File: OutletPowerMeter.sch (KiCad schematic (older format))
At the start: 94 parts, among them J1 TB002-500-03BE, J2 TB002V-500-03BE, J3 OLED, J4 Programmer, J5 TB002V-500-02BE, SW1 PTS647SN70SMTR2LFS, T1 115V / 9V, U1 ESP32-DEVKITC-32D, U10 ADG3304BRUZ-REEL7, U11 VX7803-500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

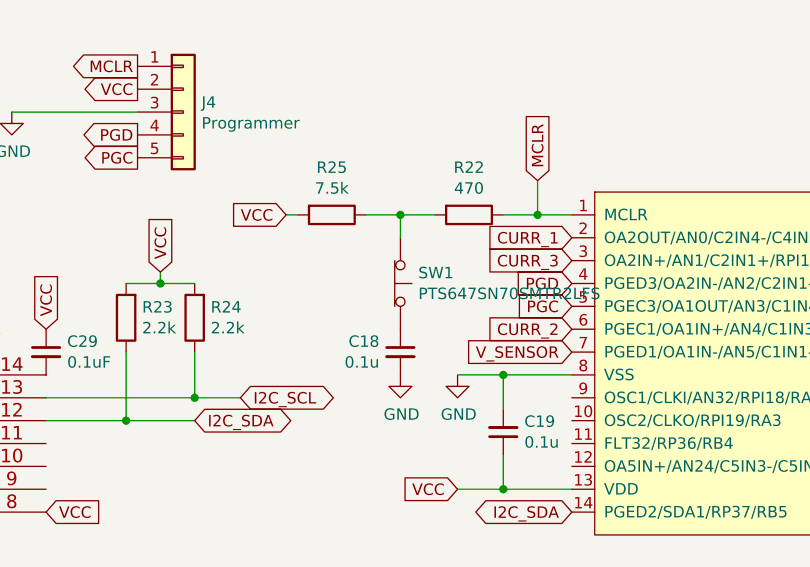
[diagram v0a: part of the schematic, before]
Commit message: Updated tactile switch and various footprints like current sensors and caps
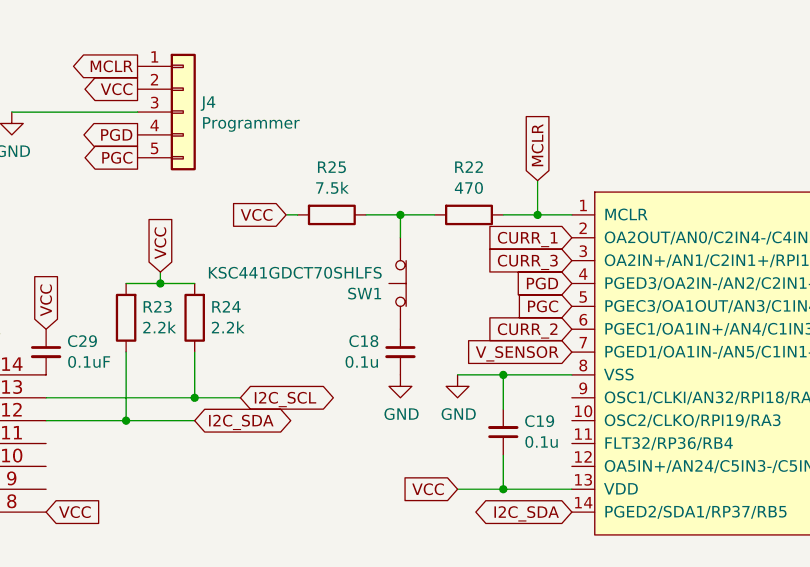
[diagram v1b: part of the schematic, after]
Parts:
- C1: footprint Capacitor_THT:C_Rect_L7.2mm_W3.5mm_P5.00mm_FKS2_FKP2_MKS2_MKP2 -> MyCustom_Footprints:C_Rect_L19.0mm_W10.0mm_P15.00mm_MKS4
- C2: footprint Capacitor_THT:C_Rect_L13.0mm_W5.0mm_P10.00mm_FKS3_FKP3_MKS4 -> Capacitor_THT:C_Rect_L7.2mm_W3.5mm_P5.00mm_FKS2_FKP2_MKS2_MKP2
- R1, R2, R3, R4, R5, R6: footprint Varistor:RV_Disc_D12mm_W3.9mm_P7.5mm -> MyCustom_Footprints:RV_Disc_D12mm_W3.9mm_P7.5mm_1.1mm
- SW1: value PTS647SN70SMTR2LFS -> KSC441GDCT70SHLFS; footprint (none) -> MyCustom_Footprints:KSC4
- U5, U6, U7: footprint SOIC-8_ALM -> Package_SO:SOIC-8_3.9x4.9mm_P1.27mm
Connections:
- net at R22.2, R25.1: now also SW1.2 (B); no longer SW1.1 (A)
- net at C18.1: now also SW1.1 (A); no longer SW1.2 (B)
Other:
- moved on the sheet: SW1
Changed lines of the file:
@@
 F 0 "R4" H 2300 2050 50  0000 R CNN
 F 1 "MOV-10D201KTR" H 2100 2600 50  0001 R CNN
-F 2 "Varistor:RV_Disc_D12mm_W3.9mm_P7.5mm" V 2080 2100 50  0001 C CNN
+F 2 "MyCustom_Footprints:RV_Disc_D12mm_W3.9mm_P7.5mm_1.1mm" V 2080 2100 50  0001 C CNN
 F 3 "~" H 2150 2100 50  0001 C CNN
 	1    2150 2100
@@
 F 0 "R1" H 1550 1750 50  0000 R CNN
 F 1 "MOV-10D201KTR" H 1350 2300 50  0001 R CNN
-F 2 "Varistor:RV_Disc_D12mm_W3.9mm_P7.5mm" V 1330 1800 50  0001 C CNN
+F 2 "MyCustom_Footprints:RV_Disc_D12mm_W3.9mm_P7.5mm_1.1mm" V 1330 1800 50  0001 C CNN
 F 3 "~" H 1400 1800 50  0001 C CNN
 	1    1400 1800
@@
 F 0 "R5" H 2550 1900 50  0000 R CNN
 F 1 "MOV-10D201KTR" H 2950 2350 50  0000 R CNN
-F 2 "Varistor:RV_Disc_D12mm_W3.9mm_P7.5mm" V 2330 1950 50  0001 C CNN
+F 2 "MyCustom_Footprints:RV_Disc_D12mm_W3.9mm_P7.5mm_1.1mm" V 2330 1950 50  0001 C CNN
 F 3 "~" H 2400 1950 50  0001 C CNN
 	1    2400 1950
@@
 F 0 "R2" H 1800 1750 50  0000 R CNN
 F 1 "MOV-10D201KTR" H 1600 2300 50  0001 R CNN
-F 2 "Varistor:RV_Disc_D12mm_W3.9mm_P7.5mm" V 1580 1800 50  0001 C CNN
+F 2 "MyCustom_Footprints:RV_Disc_D12mm_W3.9mm_P7.5mm_1.1mm" V 1580 1800 50  0001 C CNN
 F 3 "~" H 1650 1800 50  0001 C CNN
 	1    1650 1800
@@
 F 0 "R3" H 2050 2050 50  0000 R CNN
 F 1 "MOV-10D201KTR" H 1850 2600 50  0001 R CNN
-F 2 "Varistor:RV_Disc_D12mm_W3.9mm_P7.5mm" V 1830 2100 50  0001 C CNN
+F 2 "MyCustom_Footprints:RV_Disc_D12mm_W3.9mm_P7.5mm_1.1mm" V 1830 2100 50  0001 C CNN
 F 3 "~" H 1900 2100 50  0001 C CNN
 	1    1900 2100
@@
 F 0 "R6" H 2800 1900 50  0000 R CNN
 F 1 "MOV-10D201KTR" H 3200 2350 50  0001 R CNN
-F 2 "Varistor:RV_Disc_D12mm_W3.9mm_P7.5mm" V 2580 1950 50  0001 C CNN
+F 2 "MyCustom_Footprints:RV_Disc_D12mm_W3.9mm_P7.5mm_1.1mm" V 2580 1950 50  0001 C CNN
 F 3 "~" H 2650 1950 50  0001 C CNN
 	1    2650 1950
@@
 F 0 "U5" H 8700 1938 60  0000 C CNN
 F 1 "ACS712ELCTR-20A-T" H 8700 1832 60  0000 C CNN
-F 2 "SOIC-8_ALM" H 8700 1790 60  0001 C CNN
+F 2 "Package_SO:SOIC-8_3.9x4.9mm_P1.27mm" H 8700 1790 60  0001 C CNN
 F 3 "" H 7500 1550 60  0000 C CNN
 	1    7500 1550
@@
 F 0 "U6" H 8700 3438 60  0000 C CNN
 F 1 "ACS712ELCTR-20A-T" H 8700 3332 60  0000 C CNN
-F 2 "SOIC-8_ALM" H 8700 3290 60  0001 C CNN
+F 2 "Package_SO:SOIC-8_3.9x4.9mm_P1.27mm" H 8700 3290 60  0001 C CNN
 F 3 "" H 7500 3050 60  0000 C CNN
 	1    7500 3050
@@
 F 0 "U7" H 8700 5038 60  0000 C CNN
 F 1 "ACS712ELCTR-20A-T" H 8700 4932 60  0000 C CNN
-F 2 "SOIC-8_ALM" H 8700 4890 60  0001 C CNN
+F 2 "Package_SO:SOIC-8_3.9x4.9mm_P1.27mm" H 8700 4890 60  0001 C CNN
 F 3 "" H 7500 4650 60  0000 C CNN
 	1    7500 4650
@@
 F 0 "C2" H 2192 5946 50  0000 L CNN
 F 1 "6.8nF/275V" H 2192 5855 50  0000 L CNN
-F 2 "Capacitor_THT:C_Rect_L13.0mm_W5.0mm_P10.00mm_FKS3_FKP3_MKS4" H 2100 5900 50  0001 C CNN
+F 2 "Capacitor_THT:C_Rect_L7.2mm_W3.5mm_P5.00mm_FKS2_FKP2_MKS2_MKP2" H 2100 5900 50  0001 C CNN
 F 3 "~" H 2100 5900 50  0001 C CNN
 	1    2100 5900
@@
 F 0 "C1" H 1442 5946 50  0000 L CNN
 F 1 "100nF/250V" H 1442 5855 50  0000 L CNN
-F 2 "Capacitor_THT:C_Rect_L7.2mm_W3.5mm_P5.00mm_FKS2_FKP2_MKS2_MKP2" H 1350 5900 50  0001 C CNN
+F 2 "MyCustom_Footprints:C_Rect_L19.0mm_W10.0mm_P15.00mm_MKS4" H 1350 5900 50  0001 C CNN
 F 3 "~" H 1350 5900 50  0001 C CNN
 	1    1350 5900
@@
 P 6350 9200
 F 0 "SW1" V 6304 9278 50  0000 L CNN
-F 1 "PTS647SN70SMTR2LFS" V 6395 9278 50  0000 L CNN
-F 2 "" H 6350 9400 50  0001 C CNN
+F 1 "KSC441GDCT70SHLFS" V 6395 9278 50  0000 L CNN
+F 2 "MyCustom_Footprints:KSC4" H 6350 9400 50  0001 C CNN
 F 3 "~" H 6350 9400 50  0001 C CNN
 	1    6350 9200
-	0    1    1    0
+	0    -1   -1   0
 $EndComp
 Connection ~ 5450 9700

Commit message: Fixed Vcc capacitors. Added more vias.
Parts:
- removed C32: 0.1uF, Capacitor_SMD:C_0805_2012Metric_Pad1.15x1.40mm_HandSolder, symbol Device:C_Small
- added C25: 0.1uF, Capacitor_SMD:C_0805_2012Metric_Pad1.15x1.40mm_HandSolder, symbol Device:C_Small
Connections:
- net 3V3: now also U10.1 (VCCA)
- net GND: now also C24.2, C26.2, C27.1, C28.2, C29.2, C30.2, C31.2, C25.2
- net VCC: now also C24.1, C28.1, C30.1, C31.1, U1.19 (EXT_5V), U10.14 (VCCY), U5.8 (VCC), U6.8 (VCC), U7.8 (VCC), U8.8 (VDD), U9.5, C25.1; no longer C24.2, C28.2, C30.2, C31.2
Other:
- moved on the sheet: C24, C26, C27, C28, C29, C30

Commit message: Changed capacitor footprint to 1210 as well as the symbol.
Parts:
- C6: footprint Capacitor_SMD:C_1206_3216Metric_Pad1.42x1.75mm_HandSolder -> Capacitor_Tantalum_SMD:CP_EIA-3528-21_Kemet-B_Pad1.50x2.35mm_HandSolder; symbol Device:C_Small -> Device:CP1_Small
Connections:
- net at R7.2, R8.1: now also C6.1; no longer C6.2
- net at D2.3, R10.2, R11.1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: now also C6.2; no longer C6.1
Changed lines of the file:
@@
 	700  7100 700  7200
 $Comp
-L Device:C_Small C6
+L Device:CP1_Small C6
 U 1 1 5EEE7C78
 P 1050 7200
 F 0 "C6" H 1142 7246 50  0000 L CNN
 F 1 "100u" H 1142 7155 50  0000 L CNN
-F 2 "Capacitor_SMD:C_1206_3216Metric_Pad1.42x1.75mm_HandSolder" H 1050 7200 50  0001 C CNN
+F 2 "Capacitor_Tantalum_SMD:CP_EIA-3528-21_Kemet-B_Pad1.50x2.35mm_HandSolder" H 1050 7200 50  0001 C CNN
 F 3 "~" H 1050 7200 50  0001 C CNN
 	1    1050 7200
-	0    1    1    0
+	0    -1   -1   0
 $EndComp
 $Comp

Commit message: Revision 1 completed. Order sent to JLCPCB. Routed traces, rearranged components, and changed footprints.
	new file:   Gerber.zip
	modified:   OutletPowerMeter.kicad_pcb
	modified:   OutletPowerMeter.kicad_pcb-bak
	modified:   OutletPowerMeter.net
	modified:   OutletPowerMeter.sch
	modified:   OutletPowerMeter.sch-bak
	modified:   OutletPowerMeter.xml
	modified:   OutletPowerMeter.zip
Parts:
- C10, C14, C15, C16: footprint Capacitor_SMD:C_1206_3216Metric_Pad1.42x1.75mm_HandSolder -> Capacitor_SMD:C_0805_2012Metric_Pad1.15x1.40mm_HandSolder
- U10: footprint RU_14_ADI -> Package_SO:TSSOP-14_4.4x5mm_P0.65mm
- U8: footprint SOIC8-N_MC_MCH -> Package_SO:SOIC-8_3.9x4.9mm_P1.27mm
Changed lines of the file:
@@
 F 0 "C14" H 12892 1796 50  0000 L CNN
 F 1 "100n" H 12892 1705 50  0000 L CNN
-F 2 "Capacitor_SMD:C_1206_3216Metric_Pad1.42x1.75mm_HandSolder" H 12800 1750 50  0001 C CNN
+F 2 "Capacitor_SMD:C_0805_2012Metric_Pad1.15x1.40mm_HandSolder" H 12800 1750 50  0001 C CNN
 F 3 "~" H 12800 1750 50  0001 C CNN
 	1    12800 1750
@@
 F 0 "U10" H 4100 9850 60  0000 C CNN
 F 1 "ADG3304BRUZ-REEL7" H 4150 9750 60  0000 C CNN
-F 2 "RU_14_ADI" H 4650 9740 60  0001 C CNN
+F 2 "Package_SO:TSSOP-14_4.4x5mm_P0.65mm" H 4650 9740 60  0001 C CNN
 F 3 "" H 3450 9600 60  0000 C CNN
 	1    3450 9600
@@
 F 0 "U8" H 3350 3287 60  0000 C CNN
 F 1 "MCP6542T-I_SN" H 3350 3181 60  0000 C CNN
-F 2 "SOIC8-N_MC_MCH" H 3350 3140 60  0001 C CNN
+F 2 "Package_SO:SOIC-8_3.9x4.9mm_P1.27mm" H 3350 3140 60  0001 C CNN
 F 3 "" H 2550 3000 60  0000 C CNN
 	1    2550 3000
@@
 F 0 "C15" H 12892 3296 50  0000 L CNN
 F 1 "100n" H 12892 3205 50  0000 L CNN
-F 2 "Capacitor_SMD:C_1206_3216Metric_Pad1.42x1.75mm_HandSolder" H 12800 3250 50  0001 C CNN
+F 2 "Capacitor_SMD:C_0805_2012Metric_Pad1.15x1.40mm_HandSolder" H 12800 3250 50  0001 C CNN
 F 3 "~" H 12800 3250 50  0001 C CNN
 	1    12800 3250
@@
 F 0 "C16" H 12892 4896 50  0000 L CNN
 F 1 "100n" H 12892 4805 50  0000 L CNN
-F 2 "Capacitor_SMD:C_1206_3216Metric_Pad1.42x1.75mm_HandSolder" H 12800 4850 50  0001 C CNN
+F 2 "Capacitor_SMD:C_0805_2012Metric_Pad1.15x1.40mm_HandSolder" H 12800 4850 50  0001 C CNN
 F 3 "~" H 12800 4850 50  0001 C CNN
 	1    12800 4850
@@
 F 0 "C10" H 3692 7346 50  0000 L CNN
 F 1 "100n" H 3692 7255 50  0000 L CNN
-F 2 "Capacitor_SMD:C_1206_3216Metric_Pad1.42x1.75mm_HandSolder" H 3600 7300 50  0001 C CNN
+F 2 "Capacitor_SMD:C_0805_2012Metric_Pad1.15x1.40mm_HandSolder" H 3600 7300 50  0001 C CNN
 F 3 "~" H 3600 7300 50  0001 C CNN
 	1    3600 7300

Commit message: Updated schematic to make it more 'linear' and added the 27k resistors for power factor circuitry
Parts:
- added R? (x2): 27k, Resistor_SMD:R_1206_3216Metric_Pad1.42x1.75mm_HandSolder, symbol Device:R
- D1: symbol Diode_Bridge:MB2S -> Device:D_Bridge_+-AA
- J4: value Programmer -> dsPIC33 Programmer
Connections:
- net GND: now also D1.2 (-), R?.2, R?.2; no longer D1.4 (-)
- net at C22.1, C3.1, C4.1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: now also D1.1 (+); no longer D1.3 (+)
- net at C6.2, D2.3, R10.2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: now also U3.3 (+); no longer U3.2 (-)
- net at R12.2, U3.1: now also U3.2 (-); no longer U3.3 (+)
- net at D5.3, R15.1: now also U3.12 (+); no longer U3.13 (-)
- net at D4.3, R14.1: now also U3.10 (+); no longer U3.9 (-)
- net at D3.3, R13.1: now also U3.5 (+); no longer U3.6 (-)
- net at R16.2, U3.7: now also U3.6 (-); no longer U3.5 (+)
- net at R17.2, U3.8: now also U3.9 (-); no longer U3.10 (+)
- net at R18.2, U3.14: now also U3.13 (-); no longer U3.12 (+)
- net at C2.1, T1.9 (SA): now also D1.4 (~~); no longer D1.1 (~~)
- net at D6.1 (K), D8.2 (A), U8.2 (VINA-): now also R20.2, R?.1; no longer R20.1
- net at D6.2 (A), D8.1 (K), R21.2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: now also R?.1
- net 9V: no longer names the net of R7.1, T1.7 (SB), TP1.1
- net 9V: now also D1.3 (~~); no longer D1.2 (~~)
- net HOT_LEAD renamed HOT_WIRE_INPUT
- net HOT_OUT: no longer names the net of C1.1, C8.1, FL1.4, J2.2 (Pin_2), R21.1, T1.5 (AA)
- net I2C_SCL_3V3 renamed SCL_3.3V
- net SCL_3.3V: now also J3.1 (Pin_1); no longer J3.2 (Pin_2)
- net I2C_SDA_3V3 renamed SDA_3.3v
- net SDA_3.3v: now also J3.2 (Pin_2); no longer J3.1 (Pin_1)
- net NEUTRAL_OUT: no longer names the net of U5.3 (IP-), U5.4 (IP-), U6.3 (IP-), U6.4 (IP-), U7.3 (IP-), U7.4 (IP-)
- net NEUTRAL_OUT: now also D7.2 (A), D9.1 (K), R19.2, U8.5 (VINB+); no longer D7.1 (K), D9.2 (A), R19.1, U8.6 (VINB-)
- removed net NEUTRAL_SURGE: C9.2, D7.2 (A), D9.1 (K), FL1.3, R19.2, R20.2, T1.1 (AB), U8.5 (VINB+)
- net NEUT_1 renamed NEUTRAL_1
- net NEUT_2 renamed NEUTRAL_2
- net NEUT_3 renamed NEUTRAL_3
- new net: C9.2, D7.1 (K), D9.2 (A), FL1.3, R19.1, R20.1, T1.1 (AB), U8.6 (VINB-)
- no-connect marks 0 -> 50
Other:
- note added: "3.3V/5V LEVEL SHIFTER"
- note added: "CURRENT SENSING"
- note added: "MICROCONTROLLERS"
- note added: "VOLTAGE SENSING"
- note removed: "OUTPUT"
- moved on the sheet: C1, C10, C11, C12, C13, C14, C15, C16, C17, C18, C19, C2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
